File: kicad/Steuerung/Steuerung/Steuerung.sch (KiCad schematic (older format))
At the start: 2 parts

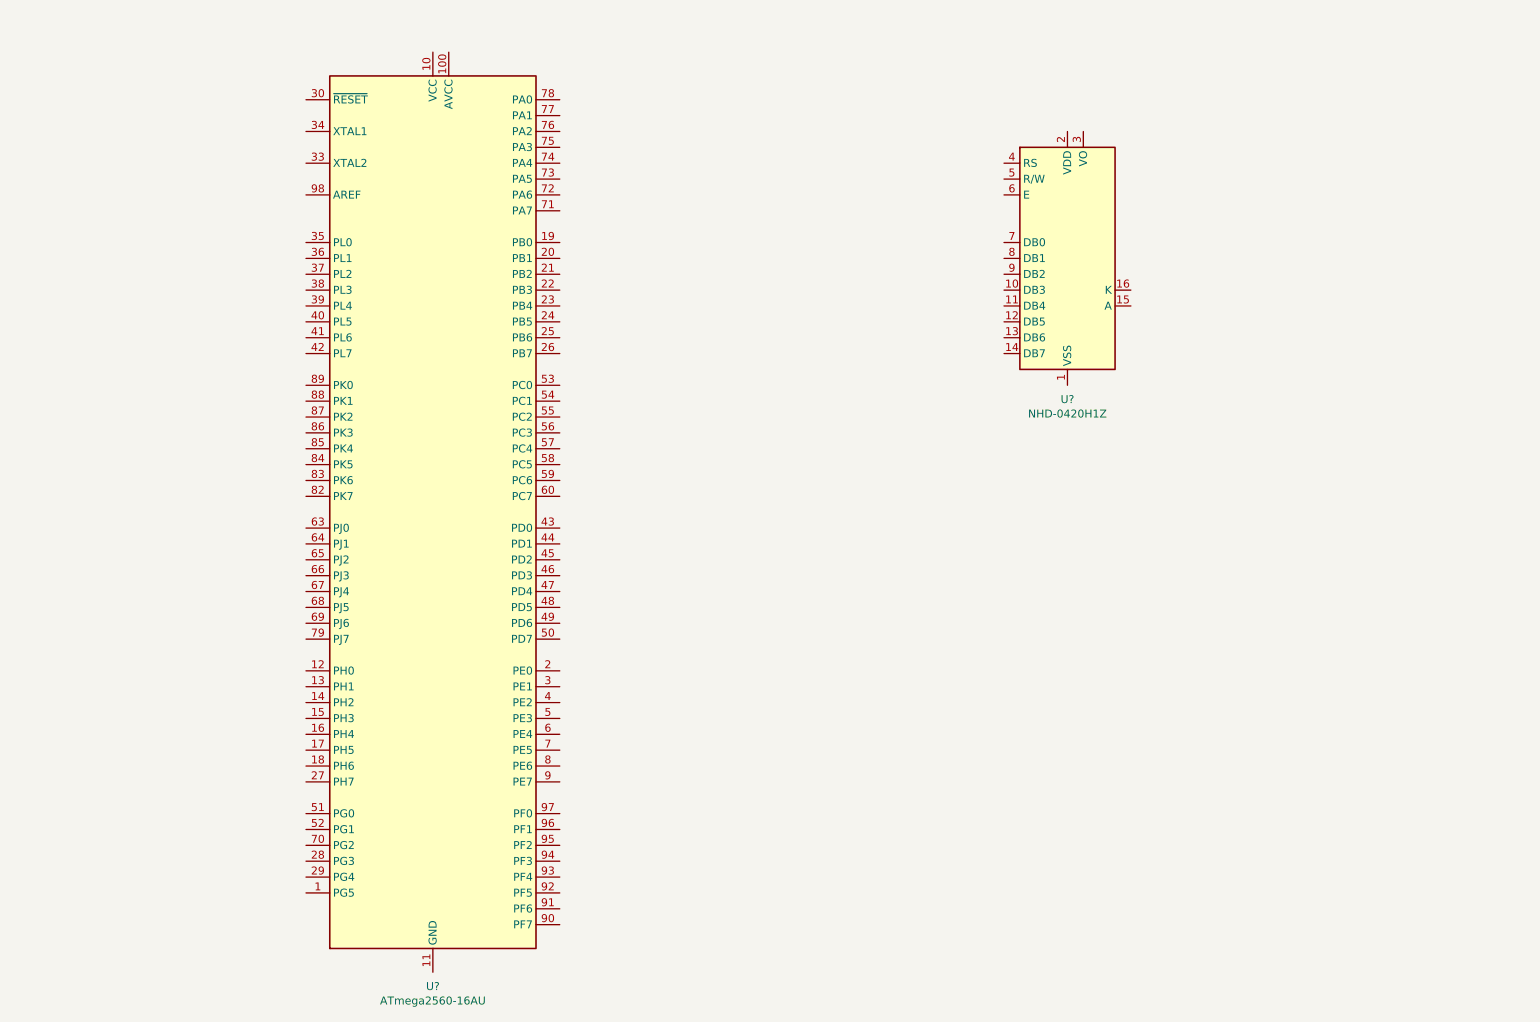
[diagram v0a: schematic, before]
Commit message: geändert:       kicad/Steuerung/Steuerung/Steuerung-cache.lib 	geändert:       kicad/Steuerung/Steuerung/Steuerung.bak 	geändert:       kicad/Steuerung/Steuerung/Steuerung.pdf 	geändert:       kicad/Steuerung/Steuerung/Steuerung.sch 	neue Datei:     librecad/aufbau/schematischer_aufbau.dxf~ 	neue Datei:     librecad/aufbau/schematischer_aufbau_versorgung.dxf 	neue Datei:     librecad/aufbau/schematischer_aufbau_versorgung.dxf~ 	neue Datei:     qelectrotech/verdrahtung/schematische_beschaltung.pdf 	neue Datei:     qelectrotech/verdrahtung/schematische_beschaltung.qet
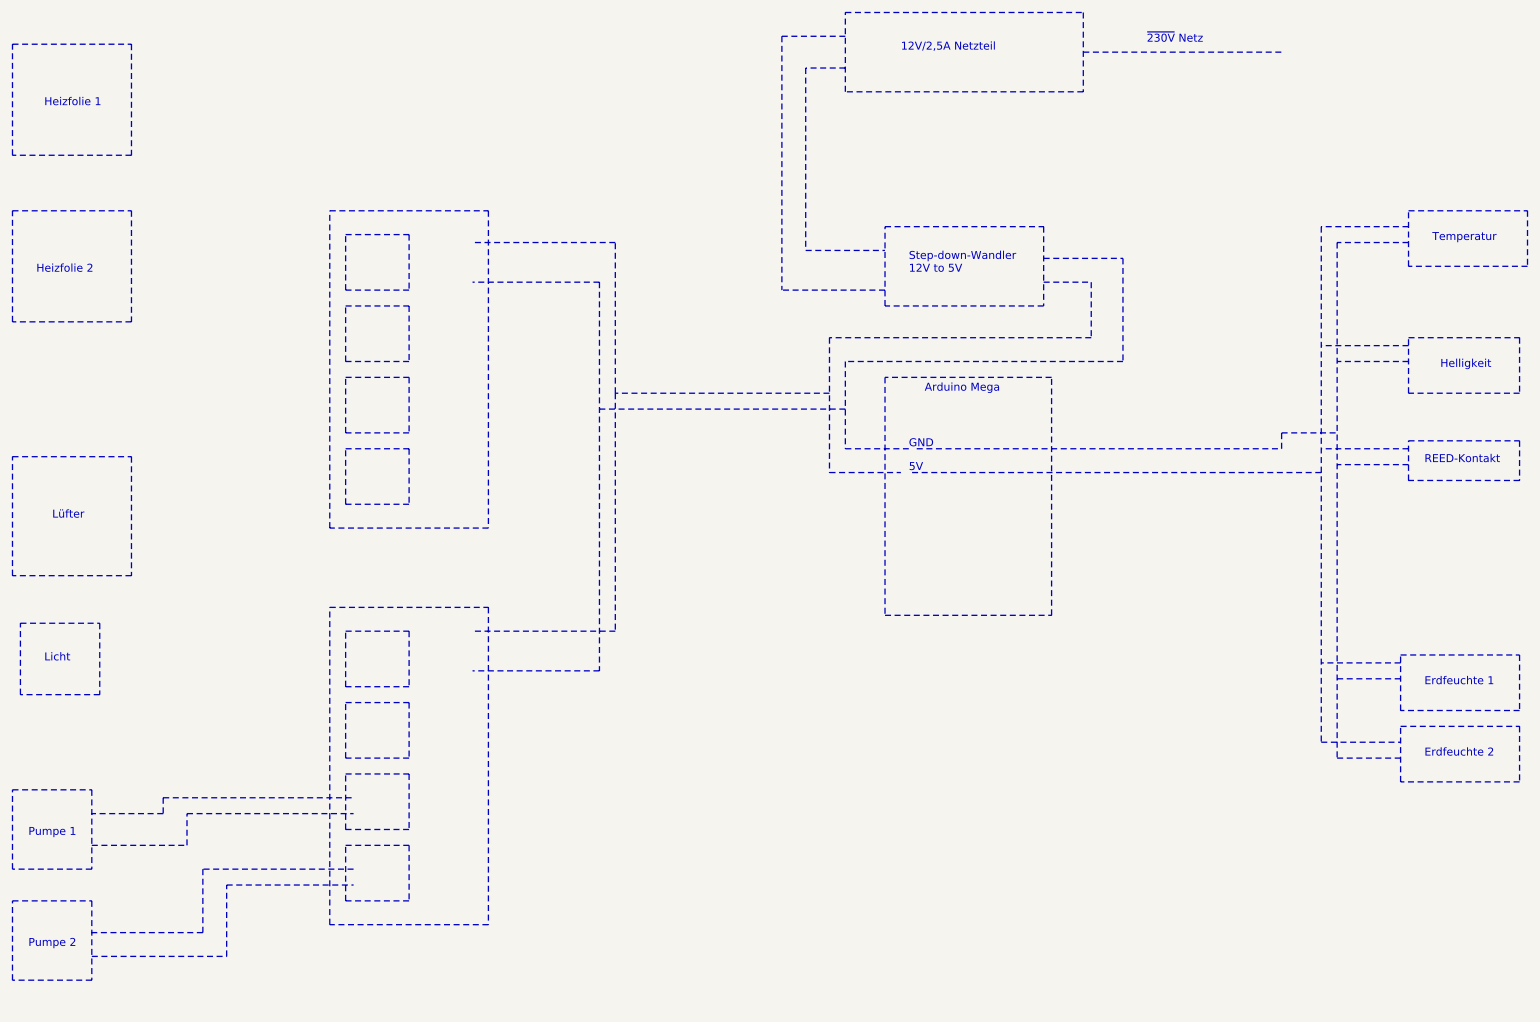
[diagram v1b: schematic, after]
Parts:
- removed U?: ATmega2560-16AU, Package_QFP:TQFP-100_14x14mm_P0.5mm, symbol MCU_Microchip_ATmega:ATmega2560-16AU
- removed U?: NHD-0420H1Z, Display:NHD-0420H1Z, symbol Display_Character:NHD-0420H1Z
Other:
- note added: "12V/2,5A Netzteil"
- note added: "5V"
- note added: "Arduino Mega"
- note added: "Erdfeuchte 1"
- note added: "Erdfeuchte 2"
- note added: "GND"
- note added: "Heizfolie 1"
- note added: "Heizfolie 2"
- note added: "Helligkeit"
- note added: "Licht"
- note added: "Lüfter"
- note added: "Pumpe 1"
- note added: "Pumpe 2"
- note added: "REED-Kontakt"
- note added: "Step-down-Wandler\n12V to 5V"
- note added: "Temperatur"
- note added: "~230V Netz"
